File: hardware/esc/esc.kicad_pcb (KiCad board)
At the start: 6 copper layers, 38 x 41.5 mm, 225 parts, among them J1 TO_FC, J10 PHASE_A, J11 PHASE_B, J12 PHASE_C, J13 PHASE_A, J14 PHASE_B, J15 PHASE_C, J2 BAT_IN, J3 BAT_GND, J4 PHASE_A, J5 PHASE_B, J6 PHASE_C, J7 PHASE_A, J8 PHASE_B, J9 PHASE_C, Q1 NVTFWS003N04XMTAG, Q10 NVTFWS003N04XMTAG, Q11 NVTFWS003N04XMTAG, Q12 NVTFWS003N04XMTAG, Q13 NVTFWS003N04XMTAG, Q14 NVTFWS003N04XMTAG, Q15 NVTFWS003N04XMTAG, Q16 NVTFWS003N04XMTAG, Q17 NVTFWS003N04XMTAG, Q18 NVTFWS003N04XMTAG, Q19 NVTFWS003N04XMTAG, Q2 NVTFWS003N04XMTAG, Q20 NVTFWS003N04XMTAG, Q21 NVTFWS003N04XMTAG, Q22 NVTFWS003N04XMTAG, Q23 NVTFWS003N04XMTAG, Q24 NVTFWS003N04XMTAG, Q3 NVTFWS003N04XMTAG, Q4 NVTFWS003N04XMTAG, Q5 NVTFWS003N04XMTAG, Q6 NVTFWS003N04XMTAG, Q7 NVTFWS003N04XMTAG, Q8 NVTFWS003N04XMTAG, Q9 NVTFWS003N04XMTAG, U1 DRV8300DRGER, U10 DRV8300DRGER, U11 STM32G071K8U6, U12 INA180A1, U13 TPS56339DDC, U14 NCP59800BMNADJTAG, U2 NCP59800BMNADJTAG, U2 STM32G071K8U6, U3 INA180A1, U4 DRV8300DRGER, U5 STM32G071K8U6, U6 INA180A1, U7 DRV8300DRGER, U8 STM32G071K8U6, U9 INA180A1

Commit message: h/feat: power stage
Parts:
- removed the C13 at (169.7, 105.3)
- removed the C6 at (169.7, 107.2)
- removed R4: 31.6k, Resistor_SMD:R_0402_1005Metric
- removed the R5 at (174.9, 107.5)
- removed the U2 at (172.3, 106.4)
- C41, C43, R74, R76, U14: moved to B.Cu
- moved R74 119.9 mm to (176.0, 107.6), turned to -90 degrees
- moved R76 117.2 mm to (174.9, 107.6), turned to -90 degrees
- moved C41 116.7 mm to (169.7, 107.3), turned to 90 degrees
- moved C43 115.0 mm to (169.7, 105.3), turned to -90 degrees
- moved U14 110.6 mm to (172.3, 106.5), turned to 180 degrees
- moved R23 2.08 mm to (168.7, 88.3)
- moved R24 2.08 mm to (170.8, 88.3)
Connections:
- U11 pad 13: SNS_BAT -> unconnected-(U11-PA6-Pad13)
- U2 pad 13: SNS_BAT -> unconnected-(U2-PA6-Pad13)
- U5 pad 13: SNS_BAT -> unconnected-(U5-PA6-Pad13)
- U8 pad 13: SNS_BAT -> unconnected-(U8-PA6-Pad13)
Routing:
- net SNS_BAT: track 15.9 -> 0.00 mm, vias 1 -> 0
- net V_5V: track 0.00 -> 4.80 mm, vias 3 -> 2
- net Net-(U13-FB): track 0.00 -> 4.67 mm
- net GND: track 13.4 -> 10.2 mm, vias 38 -> 37
- net Net-(U2-FB/SNS): track 2.81 -> 0.00 mm
- net Net-(U14-FB/SNS): track 0.00 -> 2.81 mm
- net /ESC Module 2/V_FET: track 10.5 -> 13.2 mm
- net /ESC Module 2/PHASE_A: track 17.2 -> 15.1 mm
- net /ESC Module 2/BEMF_A: track 3.52 -> 1.44 mm
- net Net-(U13-BOOT): track 0.00 -> 1.31 mm
- net Net-(U14-NR): track 0.00 -> 1.24 mm
- net Net-(U2-NR): track 1.22 -> 0.00 mm
- net /ESC Module 2/VIRTUAL: track 18.9 -> 20.1 mm
- net /M2: track 11.3 -> 10.1 mm
- net Net-(Q11-G): track 13.6 -> 12.9 mm
- added copper zone on B.Cu, net Net-(U13-SW)
- added copper zone on B.Cu, net V_5V
- added copper zone on B.Cu, net V_BAT
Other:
- outline, holes or cut-outs redrawn
- copper layers 6 -> 8

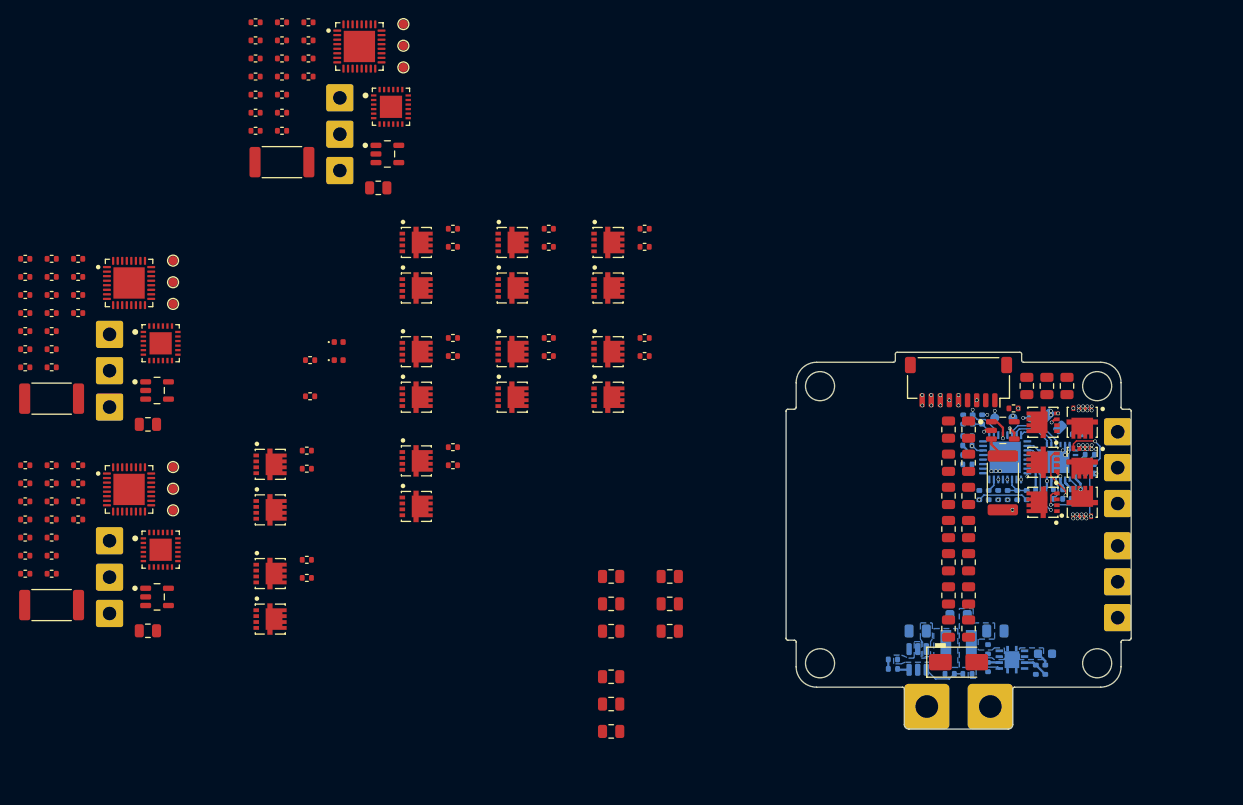
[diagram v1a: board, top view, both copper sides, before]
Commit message: h/feat: placement; power stage pending
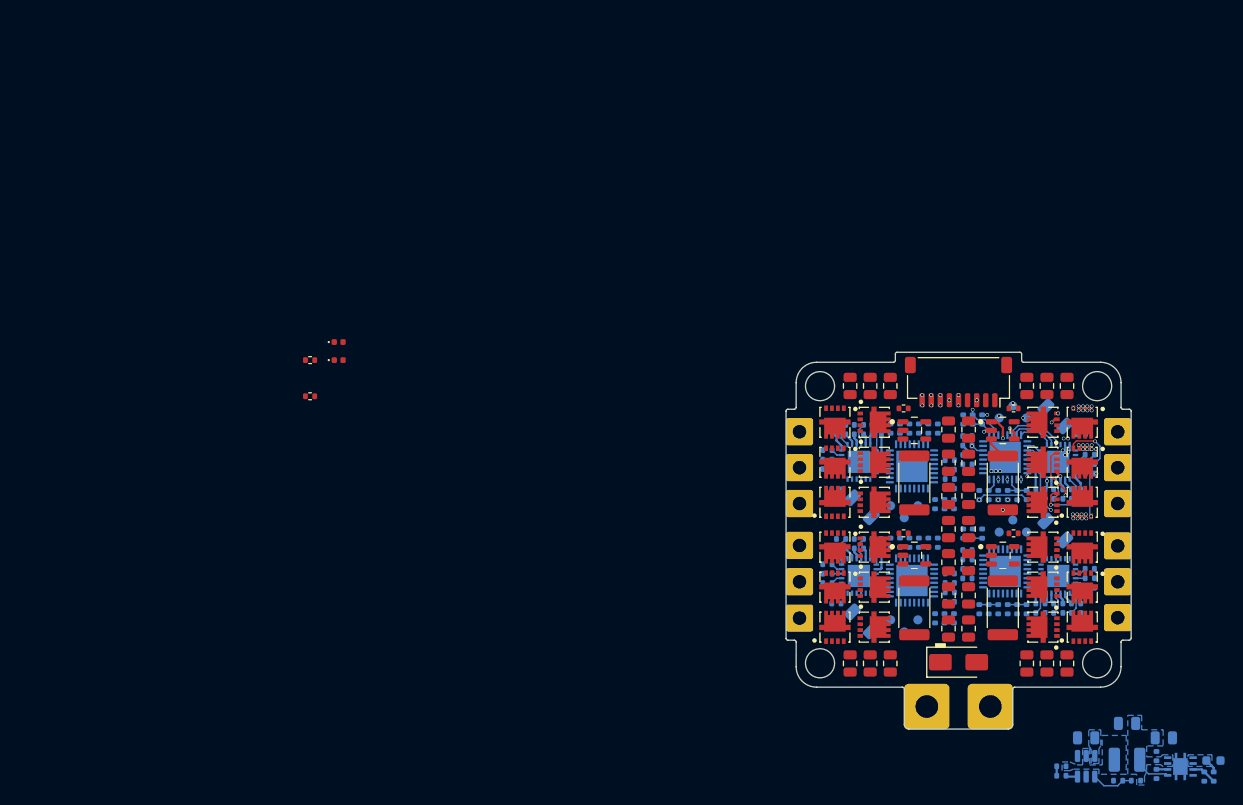
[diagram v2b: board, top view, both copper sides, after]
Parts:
- removed the J7 at (183.9, 93.9)
- removed the J8 at (183.9, 97.9)
- removed the J9 at (183.9, 101.8)
- removed L1: 4.7uH, Inductor_SMD:L_Taiyo-Yuden_MD-4040
- added REF**: L_1210_3225Metric, Inductor_SMD:L_1210_3225Metric, B.Cu at (185.0, 117.5)
- C16: footprint Capacitor_SMD:C_0805_2012Metric -> Capacitor_SMD:C_1206_3216Metric
- C2, C20, C21, C22, C23, C24, C26, C27, C29, C3, C30, C31, C32, C33, C35, C36, C4, C5, C6, C8, C9, J13, J14, J15, R11, R12, R13, R14, R15, R16, R17, R18, R19, R20, R21, R39, R40, R41, R42, R43, R45, R46, R47, R48, R49, R5, R50, R51, R52, R53, R54, R55, R56, R57, R58, R59, R6, R60, R62, R63, R64, R65, R66, R67, R68, R69, R7, R70, R71, R72, R8, R9, TP1, TP10, TP11, TP13, TP14, TP15, TP2, TP3, TP9, U1, U10, U11, U2, U7, U8: moved to B.Cu
- C25, C34, C7: footprint Capacitor_SMD:C_0805_2012Metric -> Capacitor_SMD:C_1206_3216Metric; moved to B.Cu
- moved C32 105.7 mm to (177.4, 100.3)
- moved C35 105.2 mm to (179.4, 100.3)
- moved C31 105.2 mm to (175.4, 100.3)
- moved C2 104.1 mm to (165.5, 84.5)
- moved C3 103.9 mm to (165.5, 85.5)
- moved C33 103.7 mm to (179.9, 94.2)
- moved C9 102.6 mm to (165.5, 87.6)
- moved C20 102.5 mm to (165.5, 97.0)
- moved C21 102.3 mm to (165.5, 98.0)
- moved C27 101.8 mm to (165.5, 100.1)
- moved R5 101.3 mm to (165.5, 86.6)
- moved R59 99.6 mm to (173.9, 100.9), turned to -90 degrees
- moved R39 99.6 mm to (165.5, 99.0)
- moved C29 99.4 mm to (167.4, 97.5), turned to 180 degrees
- moved R11 99.4 mm to (164.9, 89.3), turned to -90 degrees
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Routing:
- net /ESC Module 3/GHA: track 0.00 -> 3.06 mm
- net /ESC Module 1/GHA: track 0.00 -> 3.06 mm
- net /ESC Module 4/GHA: track 0.00 -> 3.06 mm
- net Net-(U1-BSTA): track 0.00 -> 2.82 mm
- net Net-(U10-BSTA): track 0.00 -> 2.82 mm
- net Net-(U7-BSTA): track 0.00 -> 2.81 mm
- net /ESC Module 3/GHC: track 0.00 -> 2.68 mm
- net /ESC Module 1/GHC: track 0.00 -> 2.68 mm
- net /ESC Module 4/GHC: track 0.00 -> 2.68 mm
- net /ESC Module 3/GHB: track 0.00 -> 2.48 mm
- net /ESC Module 1/GHB: track 0.00 -> 2.48 mm
- net /ESC Module 4/GHB: track 0.00 -> 2.48 mm
- net /ESC Module 4/BEMF_C: track 0.00 -> 2.08 mm
- net /ESC Module 4/BEMF_B: track 0.00 -> 2.08 mm
- net /ESC Module 4/BEMF_A: track 0.00 -> 2.08 mm
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
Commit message: h/feat: power stage; finalise placement
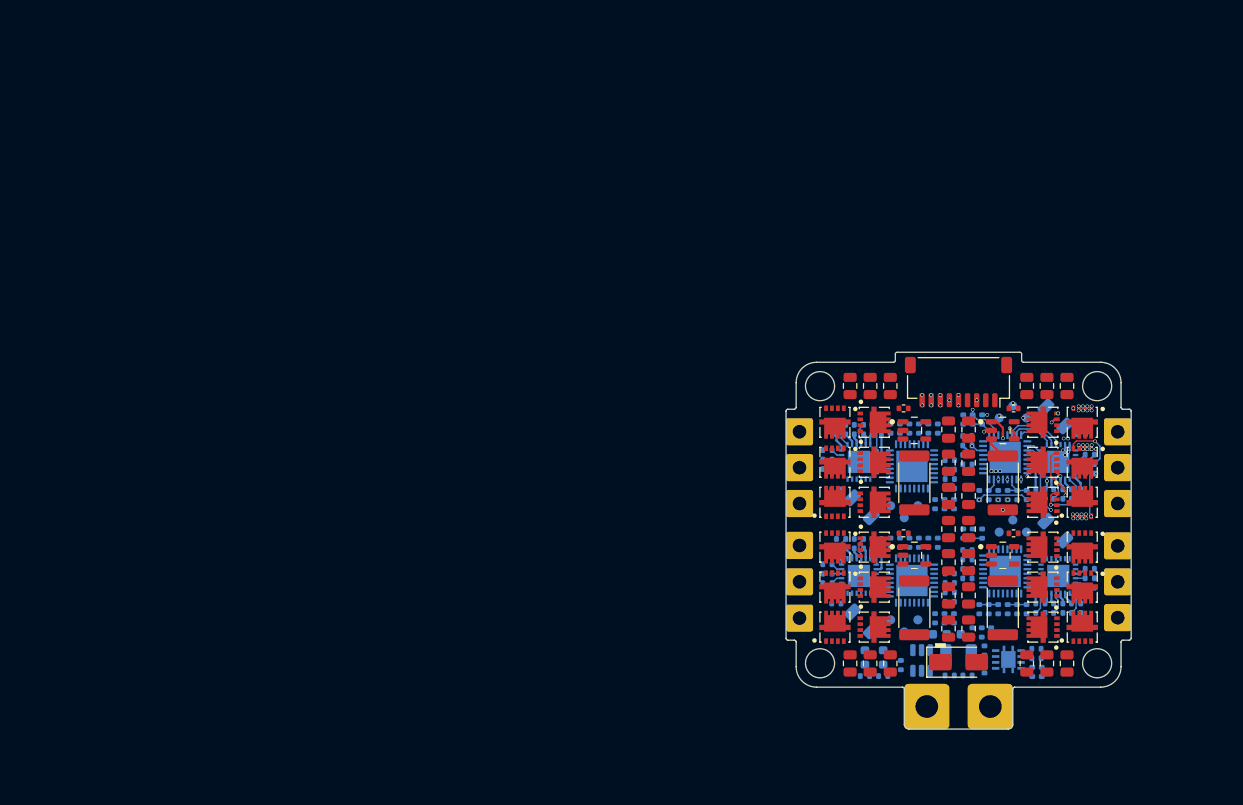
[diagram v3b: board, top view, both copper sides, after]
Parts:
- removed C38: 22uF, Capacitor_SMD:C_0805_2012Metric
- removed R73: 30R, Stratus:R_0402
- removed REF**: L_1210_3225Metric, Inductor_SMD:L_1210_3225Metric
- added C66: 10uF, Capacitor_SMD:C_0603_1608Metric, B.Cu at (162.8, 103.7)
- added C67: 10uF, Capacitor_SMD:C_0603_1608Metric, B.Cu at (165.9, 103.7)
- added C68: 10uF, Stratus:C_0402, B.Cu at (169.0, 103.5)
- added C69: 10uF, Stratus:C_0402, B.Cu at (175.0, 105.3)
- added L1: 4.7uH, Inductor_SMD:L_1210_3225Metric, B.Cu at (166.4, 106.1)
- C13, C14, C17, C22, C23, C26, C31, C32, C35, C4, C5, C8: value 0.1uF -> 1uF
- C40: value 22uF -> 10uF; footprint Capacitor_SMD:C_0603_1608Metric -> Stratus:C_0402
- C42, C65: value 22uF -> 10uF; footprint Capacitor_SMD:C_0805_2012Metric -> Stratus:C_0402
- D1, D2: footprint LED_SMD:LED_0402_1005Metric -> LED_SMD:LED_0603_1608Metric; moved to B.Cu
- R1, R3: moved to B.Cu
- R16, R17, R18, R19, R20, R21, R33, R34, R35, R36, R37, R38, R50, R51, R52, R53, R54, R55, R67, R68, R69, R70, R71, R72: value 24R -> 27R
- R75: value 56k -> 75k
- U13: value TPS56339DDC -> LMR51420YFDDCR; footprint Stratus:TPS56339DDC -> Stratus:LMR51420YFDDCR
- moved R1 70.3 mm to (156.1, 108.3), turned to 180 degrees
- moved R3 70.2 mm to (158.1, 108.3), turned to 180 degrees
- moved D2 68.3 mm to (158.1, 106.2), turned to -90 degrees
- moved D1 67.5 mm to (156.1, 106.2), turned to -90 degrees
- moved C42 24.1 mm to (167.9, 103.5), turned to 90 degrees
- moved C40 22.5 mm to (175.0, 106.3)
- moved U14 22.3 mm to (171.9, 106.4)
- moved C41 22.2 mm to (169.3, 107.4)
- moved C43 22.2 mm to (169.3, 105.4)
- moved R76 22.2 mm to (174.5, 107.8)
- moved R74 22.2 mm to (175.6, 107.8)
- moved R77 21.9 mm to (165.5, 108.2)
- moved R75 21.9 mm to (167.4, 108.2)
- moved U13 21.5 mm to (162.3, 106.5)
- moved C39 20.9 mm to (160.1, 107.1), turned to 90 degrees
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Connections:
- C39 pad 1: Net-(C39-Pad1) -> Net-(U13-BOOT)
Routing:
- net V_5V: track 4.80 -> 0.00 mm
- net Net-(U13-FB): track 4.67 -> 0.00 mm
- net Net-(U14-FB/SNS): track 2.81 -> 0.00 mm
- net V_3V3: track 3.05 -> 1.46 mm
- net Net-(U13-BOOT): track 1.31 -> 0.00 mm
- net Net-(U14-NR): track 1.24 -> 0.02 mm
- net Net-(C39-Pad1): track 1.04 -> 0.00 mm
- removed copper zone on B.Cu, net Net-(U13-SW)
- removed copper zone on B.Cu, net V_3V3
- removed copper zone on B.Cu, net V_5V
- removed copper zone on B.Cu, net V_BAT

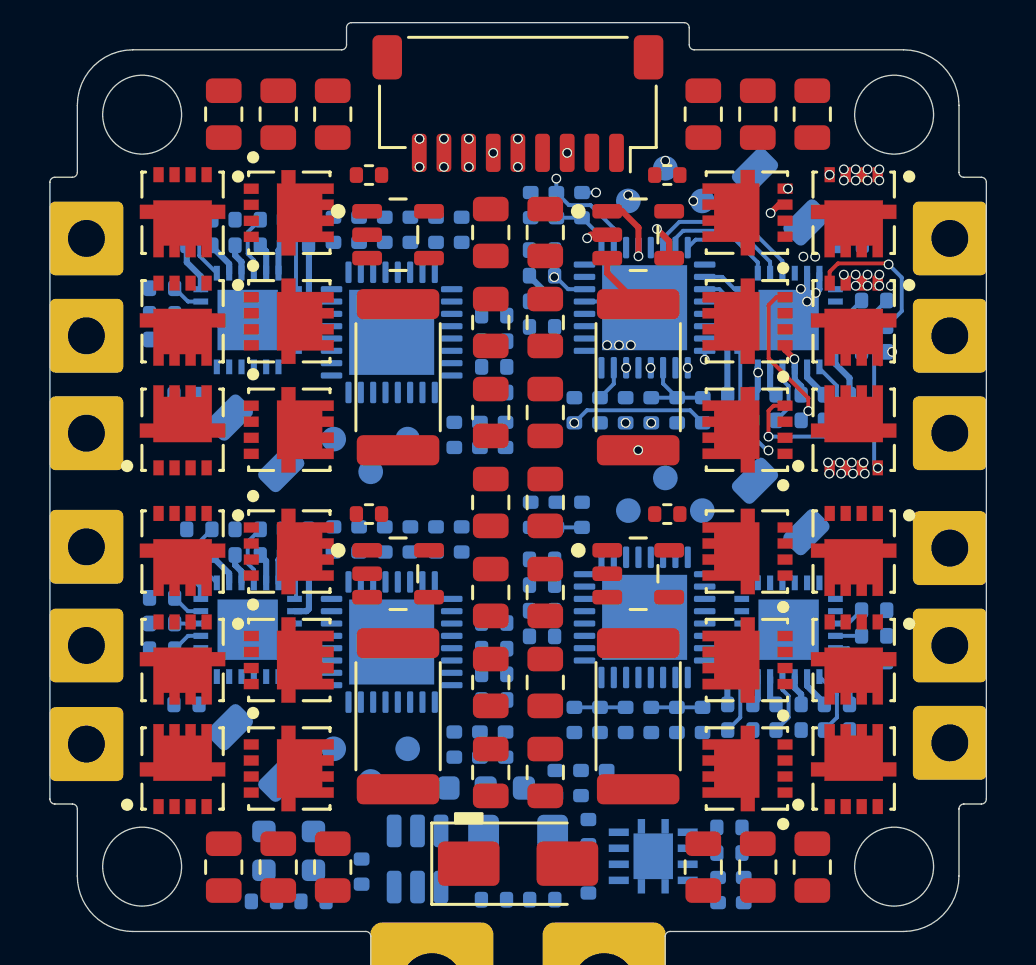
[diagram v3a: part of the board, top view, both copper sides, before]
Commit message: h/feat: 2/4 escs
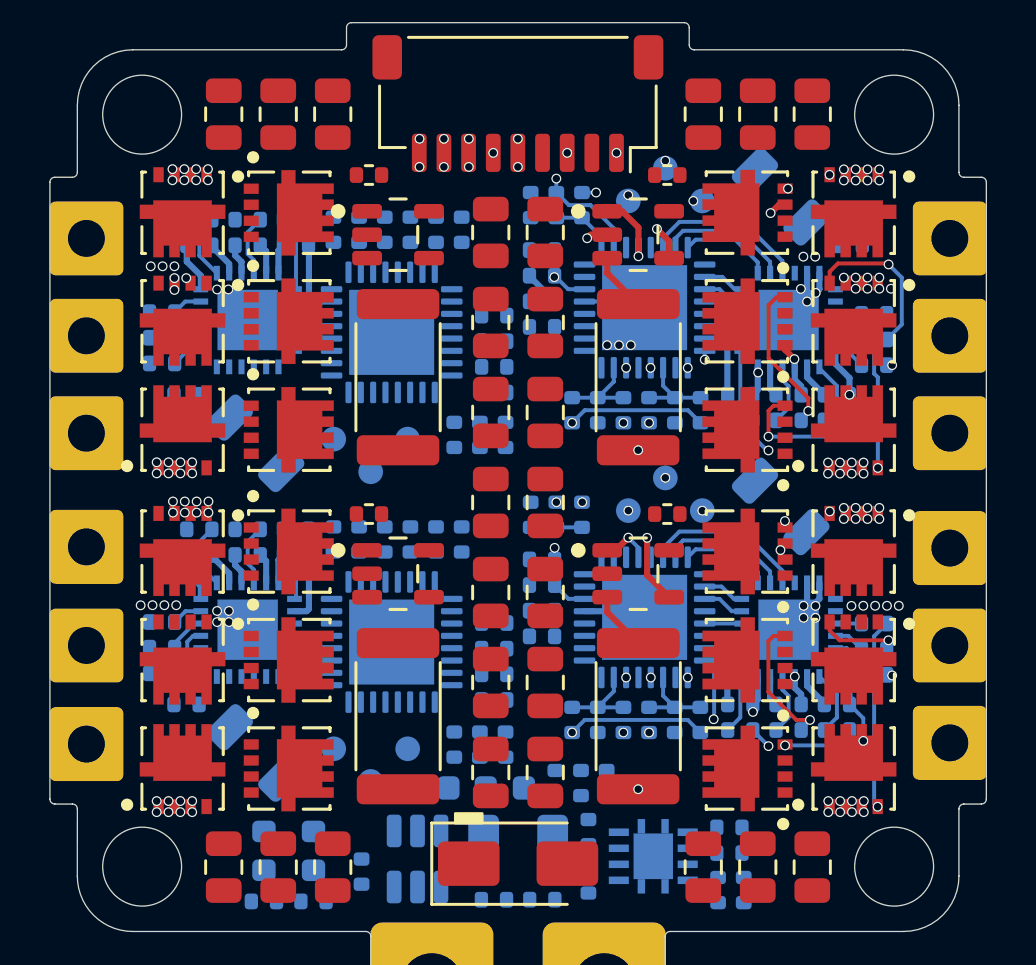
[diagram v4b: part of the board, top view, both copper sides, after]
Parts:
- moved R53 0.98 mm to (152.0, 99.0)
- moved R55 0.98 mm to (152.0, 96.9)
- moved R51 0.98 mm to (152.0, 98.0)
- moved R19 0.97 mm to (152.0, 85.4)
- moved R21 0.97 mm to (152.0, 86.4)
- moved R17 0.97 mm to (152.0, 84.4)
- moved R36 0.54 mm to (180.9, 84.4)
- moved R38 0.54 mm to (180.9, 86.5)
- moved R68 0.54 mm to (180.9, 98.0)
- moved R70 0.54 mm to (180.9, 97.0)
- moved R34 0.54 mm to (180.9, 85.5)
- moved R72 0.54 mm to (180.9, 99.1)
- moved R23 0.09 mm to (168.6, 88.3)
- moved R24 0.09 mm to (170.7, 88.3)
- moved R26 0.09 mm to (171.7, 88.3)
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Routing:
- net /M4: track 0.00 -> 22.7 mm, vias 0 -> 2
- net TELEM: track 11.2 -> 29.3 mm, vias 2 -> 3
- net /ESC Module 4/PHASE_C: track 2.02 -> 19.4 mm, vias 0 -> 2
- net /ESC Module 4/VIRTUAL: track 0.00 -> 15.2 mm, vias 0 -> 2
- net /ESC Module 4/V_FET: track 0.00 -> 14.0 mm, vias 0 -> 2
- net /ESC Module 4/PHASE_A: track 1.21 -> 14.9 mm, vias 0 -> 3
- net /ESC Module 4/SWDIO: track 0.00 -> 11.2 mm, vias 0 -> 2
- net Net-(Q23-G): track 0.00 -> 10.8 mm, vias 0 -> 2
- net GND: track 10.2 -> 19.4 mm, vias 35 -> 108
- net /ESC Module 4/SWCLK: track 0.00 -> 8.05 mm, vias 0 -> 2
- net Net-(Q24-G): track 0.00 -> 8.01 mm, vias 0 -> 2
- net Net-(Q22-G): track 0.00 -> 7.71 mm, vias 0 -> 1
- net /ESC Module 4/nRST: track 0.00 -> 7.59 mm, vias 0 -> 2
- net /ESC Module 4/PHASE_B: track 1.24 -> 8.09 mm, vias 0 -> 2
- net /ESC Module 4/LC: track 0.00 -> 6.64 mm
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
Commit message: h/feat: finalise power stage
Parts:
- moved C76 0.55 mm to (159.5, 106.9)
- moved C77 0.55 mm to (157.2, 106.9)
- moved C79 0.55 mm to (177.8, 106.9)
- moved C80 0.55 mm to (175.6, 106.9)
- moved C81 0.55 mm to (173.4, 106.9)
- moved C78 0.55 mm to (155.0, 106.9)
- moved R13 0.09 mm to (163.2, 81.0)
- moved R14 0.09 mm to (160.1, 81.0)
- moved R40 0.09 mm to (164.2, 93.6)
- moved R41 0.09 mm to (162.2, 93.6)
- moved R42 0.09 mm to (159.0, 93.6)
- moved R43 0.09 mm to (161.1, 93.6)
- moved R47 0.09 mm to (163.2, 93.6)
- moved R48 0.09 mm to (160.1, 93.6)
- moved R6 0.09 mm to (164.2, 81.0)
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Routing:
- net V_5V: track 0.00 -> 13.6 mm
- net Net-(U13-FB): track 0.00 -> 3.84 mm
- net Net-(U14-FB/SNS): track 0.00 -> 2.92 mm
- net V_3V3: track 1.46 -> 3.37 mm, vias 0 -> 4
- net GND: track 19.4 -> 21.2 mm, vias 108 -> 120
- net Net-(D2-A): track 0.00 -> 1.47 mm
- net Net-(D1-A): track 0.00 -> 1.47 mm
- net Net-(U13-BOOT): track 0.00 -> 1.37 mm
- net Net-(U14-NR): track 0.02 -> 1.31 mm
- net V_BAT: track 4.77 -> 4.79 mm, vias 2 -> 3
- added copper zone on B.Cu, net Net-(U13-SW)
- added copper zone on B.Cu, net V_3V3
- added copper zone on B.Cu, net V_5V
- added copper zone on B.Cu, net V_BAT
